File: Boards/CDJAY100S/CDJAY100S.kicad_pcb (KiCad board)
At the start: 2 copper layers, 150 x 185 mm, 54 parts, among them SW1 Rotary Encoder, U1 HT1632C-52LQFP

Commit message: Hide some details
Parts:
- moved C10 13.5 mm to (81.5, 32.1), turned to 90 degrees
- moved C9 11.0 mm to (86.0, 32.1), turned to 90 degrees
- moved R9 5.52 mm to (77.0, 32.0)
- moved R10 5.02 mm to (72.5, 32.0)
- moved R11 3.53 mm to (91.0, 32.0)
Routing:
- net Net-(rPi1-GPIO5): track 84.2 -> 96.7 mm
- net /GNDD: track 459.6 -> 447.1 mm
- net Net-(R11-Pad1): track 8.59 -> 12.5 mm
- net Net-(rPi1-GPIO4): track 87.6 -> 83.9 mm
- net Net-(rPi1-GPIO6): track 75.8 -> 72.3 mm
- net Net-(R9-Pad2): track 8.62 -> 7.10 mm
- net Net-(ControlJack1-Pin_2): track 77.8 -> 78.9 mm
- net Net-(ControlJack1-Pin_1): track 86.0 -> 87.0 mm

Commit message: Revision 1.1 of the PCB and Schematics.
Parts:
- removed C10, C9: 100 u, Capacitor_SMD:C_1206_3216Metric_Pad1.33x1.80mm_HandSolder
- removed C18: 47 u, Capacitor_SMD:C_1206_3216Metric_Pad1.33x1.80mm_HandSolder
- removed CR1: MBR120VLSFT1G, footprints:SDO_SOD-123FL_ONS
- removed Control: , Connector_Hirose:Hirose_DF13-02P-1.25DSA_1x02_P1.25mm_Vertical
- removed DSPB_Conn1: Conn_02x18_Odd_Even, 52045-3645:ConnectorFPC&FFC_MOL52045-3645-36P
- removed SW1: Rotary Encoder, Connector_PinHeader_2.54mm:PinHeader_1x05_P2.54mm_Vertical
- removed TB1: Conn_01x14, Connector_PinHeader_2.00mm:PinHeader_1x14_P2.00mm_Vertical
- added C22: 100 n, Capacitor_SMD:C_1206_3216Metric_Pad1.33x1.80mm_HandSolder, F.Cu at (161.5, 133.5)
- added C23: 100 n, Capacitor_SMD:C_1206_3216Metric_Pad1.33x1.80mm_HandSolder, F.Cu at (161.5, 129.5)
- added C24: 100 n, Capacitor_SMD:C_1206_3216Metric_Pad1.33x1.80mm_HandSolder, F.Cu at (168.5, 137.5)
- added C5: 100 u, Capacitor_SMD:C_1206_3216Metric_Pad1.33x1.80mm_HandSolder, F.Cu at (188.0, 82.4)
- added C6: 100 u, Capacitor_SMD:C_1206_3216Metric_Pad1.33x1.80mm_HandSolder, F.Cu at (188.0, 89.5)
- added CN701: 52492-3620, 52045-3645:ConnectorFPC&FFC_MOL52045-3645-36P_1, F.Cu at (193.5, 124.6)
- added CN705: 52151-1410, Connector_PinHeader_2.00mm:PinHeader_1x14_P2.00mm_Vertical, F.Cu at (194.0, 90.0)
- added D13: 1SS355VM, Diode_SMD:Nexperia_CFP3_SOD-123W, F.Cu at (169.5, 80.1)
- added D14: 1SS355VM, Diode_SMD:Nexperia_CFP3_SOD-123W, F.Cu at (164.5, 84.0)
- added D15: 1SS355VM, Diode_SMD:Nexperia_CFP3_SOD-123W, F.Cu at (169.5, 84.0)
- added D16: 1SS355VM, Diode_SMD:Nexperia_CFP3_SOD-123W, F.Cu at (164.5, 80.0)
- added J1: Rotary Encoder, Connector_PinHeader_2.54mm:PinHeader_1x05_P2.54mm_Vertical, F.Cu at (76.0, 25.0)
- added R21: 10k, Resistor_SMD:R_1206_3216Metric_Pad1.30x1.75mm_HandSolder, F.Cu at (140.5, 119.2)
- added R22: 10k, Resistor_SMD:R_1206_3216Metric_Pad1.30x1.75mm_HandSolder, F.Cu at (140.6, 122.5)
- added R23: 22k, Resistor_SMD:R_1206_3216Metric_Pad1.30x1.75mm_HandSolder, F.Cu at (182.5, 39.0)
- added R32: 10k, Resistor_SMD:R_1206_3216Metric_Pad1.30x1.75mm_HandSolder, F.Cu at (181.5, 71.5)
- added R33: 10k, Resistor_SMD:R_1206_3216Metric_Pad1.30x1.75mm_HandSolder, F.Cu at (185.0, 71.5)
- added R34: 10k, Resistor_SMD:R_1206_3216Metric_Pad1.30x1.75mm_HandSolder, F.Cu at (158.9, 85.5)
- added R7: 10k, Resistor_SMD:R_1206_3216Metric_Pad1.30x1.75mm_HandSolder, F.Cu at (140.5, 112.0)
- added R8: 10k, Resistor_SMD:R_1206_3216Metric_Pad1.30x1.75mm_HandSolder, F.Cu at (140.5, 115.5)
- C14, C15: value 1 u -> 2.2 u
- CR2: footprint footprints:SDO_SOD-123FL_ONS -> Diode_SMD:Nexperia_CFP3_SOD-123W
- D10, D11, D12, D8, D9: footprint Diode_SMD:D_SOD-323F -> Diode_SMD:Nexperia_CFP3_SOD-123W
- MH1, MH2, MH3, MH4: footprint MountingHole:MountingHole_2.2mm_M2 -> MountingHole:MountingHole_4.5mm
- R10, R11, R9: value 1 k -> 10 k
- R12: value 100 k -> 2k
- R13: value 10 k -> 2k
- R14: value 10 k -> 10k
- R15: value 100 -> 10k
- U1: value HT1632C-52LQFP -> PT6324Q; footprint Package_QFP:LQFP-52_14x14mm_P1mm -> Package_QFP:QFP-52_14x14mm_P1mm_1
- moved R14 68.5 mm to (159.0, 88.0)
- moved C16 56.4 mm to (196.5, 37.0)
- moved R13 55.1 mm to (158.5, 77.5), turned to -90 degrees
- moved R12 44.7 mm to (155.5, 77.5)
- moved CR2 44.7 mm to (183.4, 32.0), turned to 0 degrees
- moved R15 41.1 mm to (140.5, 126.0)
- moved C17 33.6 mm to (147.2, 90.5)
- moved R16 28.0 mm to (148.5, 104.5), turned to 90 degrees
- moved C12 25.3 mm to (147.2, 85.1), turned to -90 degrees
- moved R20 18.1 mm to (153.5, 159.1), turned to 90 degrees
- moved C14 17.7 mm to (189.5, 37.0), turned to 90 degrees
- moved C19 14.1 mm to (150.0, 111.0)
- moved C21 12.5 mm to (161.4, 137.5)
- moved R10 11.0 mm to (83.5, 32.0)
- moved R11 10.5 mm to (80.5, 32.0), turned to 90 degrees
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- renumbered SPi_Level1 to U2
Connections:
- net /GR12 renamed Net-(D12-A)
- net /GR13 renamed Net-(D11-A)
- net /GR14 renamed Net-(D10-A)
- net /GR15 renamed Net-(D8-A)
- net Net-(SPi_Level1-A4) renamed /SPI0 CS
- net Net-(SPi_Level1-A5) renamed /SPI0 SCK
- net Net-(SPi_Level1-A6) renamed /SPI0 RX
- net Net-(SPi_Level1-A7) renamed /SPI0 TX
- net Net-(rPi1-GPIO26_ADC0) renamed /ADIN
- C11 pad 1: Net-(SPi_Level1-A8) -> +3V3
- C12 pad 1: Net-(SPi_Level1-A8) -> +3V3
- C12 pad 2: /GNDD -> GND
- C13 pad 1: Net-(SPi_Level1-A8) -> +3V3
- C15 pad 2: GND -> GNDA
- C17 pad 1: Net-(DSPB_Conn1-Pin_36) -> +5V
- C17 pad 2: /GNDD -> GND
- C19 pad 2: /GNDD -> GND
- C20 pad 2: /GNDD -> GND
- C21 pad 1: /VDD -> +5V
- C21 pad 2: /GNDD -> GND
- CR2 pad 2: Net-(DSPB_Conn1-Pin_36) -> +5V
- R1 pad 1: Net-(DSPB_Conn1-Pin_34) -> Net-(R1-Pad1)
- R1 pad 2: Net-(R1-Pad2) -> Net-(CN701-ADIN)
- R10 pad 1: Net-(rPi1-GPIO5) -> +3V3
- R10 pad 2: Net-(R10-Pad2) -> Net-(J1-DT)
- R11 pad 1: Net-(R11-Pad1) -> +3V3
- R12 pad 1: Net-(rPi1-3V3_EN) -> Net-(rPi1-GPIO15)
- R12 pad 2: Net-(rPi1-VSYS) -> Net-(CN705-CONT1)
- R13 pad 1: Net-(rPi1-GPIO18) -> Net-(rPi1-GPIO22)
- R13 pad 2: /GNDD -> Net-(CN705-CONT2)
- R14 pad 1: Net-(rPi1-VBUS) -> Net-(CN705-CONT1)
- R14 pad 2: Net-(rPi1-GPIO18) -> +5V
- R15 pad 1: Net-(SPi_Level1-OE) -> Net-(D10-K)
- R15 pad 2: /GNDD -> GND
- R17 pad 2: /DOUT -> Net-(U1-DOUT)
- R18 pad 1: /GNDD -> GND
- R19 pad 1: /VDD -> /DOUT
- R19 pad 2: /DOUT -> +5V
- R2 pad 1: Net-(R1-Pad2) -> Net-(R1-Pad1)
- R20 pad 1: /GNDD -> GND
- R3 pad 1: Net-(R1-Pad2) -> Net-(R1-Pad1)
- R5 pad 1: Net-(DSPB_Conn1-Pin_35) -> Net-(R4-Pad1)
- R5 pad 2: Net-(R4-Pad1) -> Net-(CN701-CT)
- R9 pad 1: Net-(rPi1-GPIO4) -> Net-(J1-CLK)
- R9 pad 2: Net-(R9-Pad2) -> +3V3
- U1 pad 10: /SG1 -> Net-(CN701-S1)
- U1 pad 11: /SG2 -> Net-(CN701-S2)
- U1 pad 12: /SG3 -> Net-(CN701-S3)
- U1 pad 13: /SG4 -> Net-(CN701-S4)
- U1 pad 14: /SG5 -> Net-(CN701-S5)
- U1 pad 15: /SG6 -> Net-(CN701-S6)
- U1 pad 17: /SG8 -> Net-(CN701-S8)
- U1 pad 18: /SG9 -> Net-(CN701-S9)
- U1 pad 19: /SG10 -> Net-(CN701-S10)
- U1 pad 20: /SG11 -> Net-(CN701-S11)
- U1 pad 21: /SG12 -> Net-(CN701-S12)
- U1 pad 34: /GR1 -> Net-(CN701-G1)
- U1 pad 35: /GR2 -> Net-(CN701-G2)
- U1 pad 36: /GR3 -> Net-(CN701-G3)
- U1 pad 37: /GR4 -> Net-(CN701-G4)
- U1 pad 38: /GR5 -> Net-(CN701-G5)
- U1 pad 39: /GR6 -> Net-(CN701-G6)
- U1 pad 4: /DOUT -> Net-(U1-DOUT)
- U1 pad 40: /GR7 -> Net-(CN701-G7)
- U1 pad 41: /GR8 -> Net-(CN701-G8)
- U1 pad 42: /GR9 -> Net-(CN701-G9)
- U1 pad 43: /GR10 -> Net-(CN701-G10)
- U1 pad 44: /GR11 -> Net-(CN701-G11)
- U1 pad 50: Net-(TB1-Pin_12) -> Vload
- U1 pad 51: /VDD -> +5V
- U1 pad 52: /GNDD -> GND
- U1 pad 8: /GNDD -> GND
- U1 pad 9: /VDD -> +5V
- U2 pad 10: Net-(SPi_Level1-OE) -> +3V3
- U2 pad 11: /GNDD -> GND
- U2 pad 12: /VDD -> unconnected-(U2-B8-Pad12)
- U2 pad 19: Net-(DSPB_Conn1-Pin_36) -> +5V
- U2 pad 2: Net-(SPi_Level1-A8) -> +3V3
- U2 pad 9: Net-(SPi_Level1-A8) -> unconnected-(U2-A8-Pad9)
- i2S_Audio1 pad 11: GND -> +3V3
- i2S_Audio1 pad 9: GND -> GNDA
- rPi1 pad 13: /GNDD -> GND
- rPi1 pad 18: /GNDD -> GND
- rPi1 pad 20: Net-(ControlJack1-Pin_1) -> Net-(rPi1-GPIO15)
- rPi1 pad 23: /GNDD -> GND
- rPi1 pad 24: Net-(rPi1-GPIO18) -> unconnected-(rPi1-GPIO18-Pad24)
- rPi1 pad 25: Net-(i2S_Audio1-LRCK) -> Net-(i2S_Audio1-BCK)
- rPi1 pad 26: Net-(i2S_Audio1-DIN) -> Net-(i2S_Audio1-LRCK)
- rPi1 pad 27: Net-(i2S_Audio1-BCK) -> Net-(i2S_Audio1-DIN)
- rPi1 pad 28: /GNDD -> GND
- rPi1 pad 29: Net-(ControlJack1-Pin_2) -> Net-(rPi1-GPIO22)
- rPi1 pad 3: /GNDD -> GND
- rPi1 pad 36: Net-(SPi_Level1-A8) -> +3V3
- rPi1 pad 37: Net-(rPi1-3V3_EN) -> unconnected-(rPi1-3V3_EN-Pad37)
- rPi1 pad 38: /GNDD -> GND
- rPi1 pad 40: Net-(rPi1-VBUS) -> unconnected-(rPi1-VBUS-Pad40)
- rPi1 pad 6: Net-(rPi1-GPIO4) -> Net-(J1-DT)
- rPi1 pad 7: Net-(rPi1-GPIO5) -> Net-(J1-CLK)
- rPi1 pad 8: /GNDD -> GND
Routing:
- net /GNDD: track 447.1 -> 0.00 mm, vias 4 -> 0
- net GND: track 188.3 -> 571.4 mm, vias 1 -> 12
- net +5V: track 0.00 -> 280.4 mm, vias 0 -> 5
- net +3V3: track 0.00 -> 225.2 mm, vias 0 -> 5
- net Net-(DSPB_Conn1-Pin_36): track 220.1 -> 0.00 mm, vias 3 -> 0
- net /VDD: track 134.5 -> 0.00 mm, vias 3 -> 0
- net Net-(SPi_Level1-A8): track 117.8 -> 0.00 mm, vias 1 -> 0
- net Net-(rPi1-GPIO5): track 96.7 -> 0.00 mm, vias 1 -> 0
- net Net-(TB1-Pin_12): track 94.6 -> 0.00 mm, vias 1 -> 0
- net Net-(ControlJack1-Pin_1): track 87.0 -> 0.00 mm
- net Vload: track 0.00 -> 85.0 mm, vias 0 -> 1
- net Net-(rPi1-GPIO18): track 84.3 -> 0.00 mm, vias 1 -> 0
- net Net-(J1-DT): track 0.00 -> 84.0 mm
- net Net-(rPi1-GPIO4): track 83.9 -> 0.00 mm, vias 1 -> 0
- net Net-(J1-CLK): track 0.00 -> 79.0 mm
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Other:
- outline, holes or cut-outs redrawn
- board text added: "CDJay 100 USB Mainboard V1.1 applab.fh-aachen.de Write it, load it, run it, save it Check it, change it, quick - reuse it"
- board text removed: "CDJay 100 USB Mainboard V1.0 applab.fh-aachen.de Write it, cut it, paste it, save it Load it, check it, quick - rewrite it"

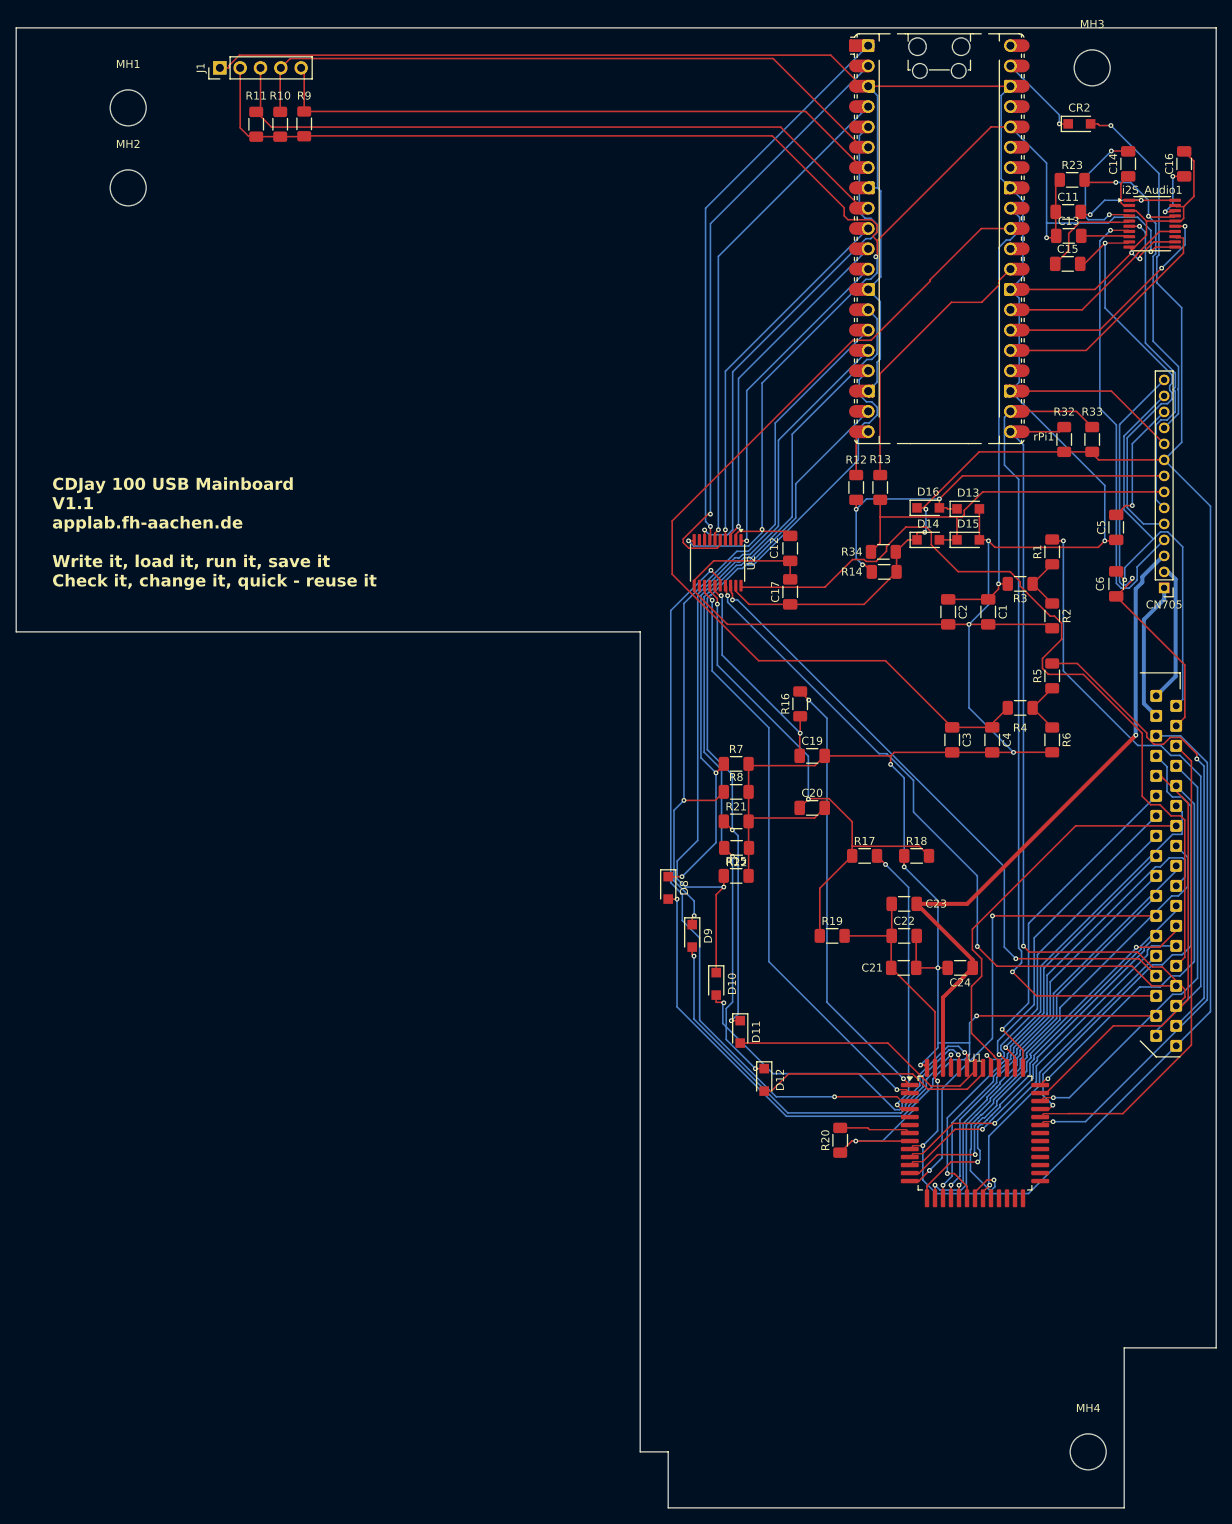
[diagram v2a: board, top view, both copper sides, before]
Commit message: Include USB-Hub
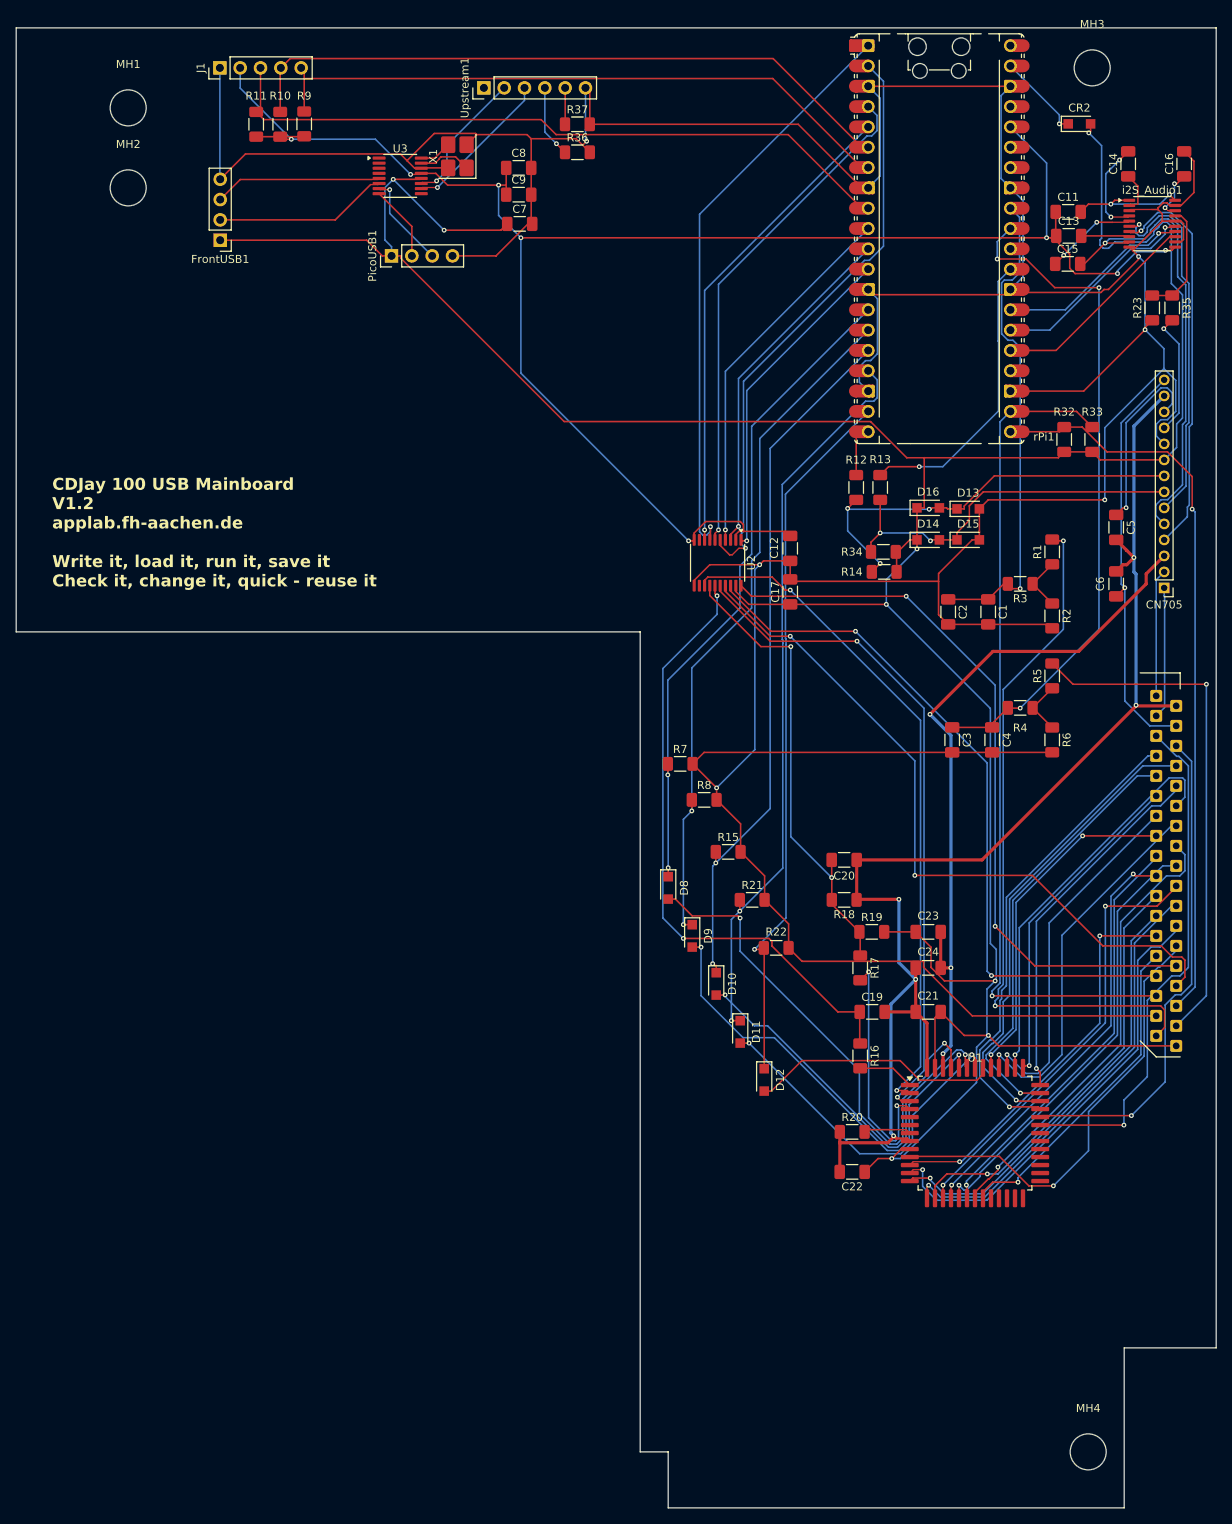
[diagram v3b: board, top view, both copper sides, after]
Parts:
- added C7: 10u, Capacitor_SMD:C_1206_3216Metric_Pad1.33x1.80mm_HandSolder, F.Cu at (113.4, 44.5)
- added C8: 10u, Capacitor_SMD:C_1206_3216Metric_Pad1.33x1.80mm_HandSolder, F.Cu at (113.3, 37.5)
- added C9: 1uf, Capacitor_SMD:C_1206_3216Metric_Pad1.33x1.80mm_HandSolder, F.Cu at (113.3, 40.9)
- added FrontUSB1: Conn_01x04_Pin, Connector_PinHeader_2.54mm:PinHeader_1x04_P2.54mm_Vertical, F.Cu at (76.0, 46.5)
- added PicoUSB1: Conn_01x04_Pin, Connector_PinHeader_2.54mm:PinHeader_1x04_P2.54mm_Vertical, F.Cu at (97.4, 48.5)
- added R35: 10k, Resistor_SMD:R_1206_3216Metric_Pad1.30x1.75mm_HandSolder, F.Cu at (195.0, 55.0)
- added R36: 5.1 k, Resistor_SMD:R_1206_3216Metric_Pad1.30x1.75mm_HandSolder, F.Cu at (120.7, 35.5)
- added R37: 5 k, Resistor_SMD:R_1206_3216Metric_Pad1.30x1.75mm_HandSolder, F.Cu at (120.7, 32.0)
- added U3: CH334R, Package_SO:QSOP-16_3.9x4.9mm_P0.635mm, F.Cu at (98.5, 38.5)
- added Upstream1: Conn_01x06_Pin, Connector_PinHeader_2.54mm:PinHeader_1x06_P2.54mm_Vertical, F.Cu at (109.0, 27.5)
- added X1: 12MHz, Crystal:Crystal_SMD_3225-4Pin_3.2x2.5mm_HandSoldering, F.Cu at (105.7, 36.0)
- R23: value 22k -> 20k
- R3, R4: value 5 k -> 5.1 k
- moved R16 44.6 mm to (156.0, 148.5), turned to -90 degrees
- moved C19 32.9 mm to (157.5, 143.0)
- moved C22 30.2 mm to (155.0, 163.0), turned to 180 degrees
- moved R23 18.9 mm to (192.5, 55.0), turned to 90 degrees
- moved R17 14.0 mm to (156.0, 137.5), turned to -90 degrees
- moved R22 13.4 mm to (145.5, 135.0)
- moved R18 10.6 mm to (154.0, 129.0), turned to 180 degrees
- moved R21 10.0 mm to (142.5, 129.0)
- moved C20 7.63 mm to (154.0, 124.0)
- moved R7 7.00 mm to (133.5, 112.0)
- moved C21 6.30 mm to (164.5, 143.0), turned to 180 degrees
- moved R19 4.98 mm to (157.4, 133.0)
- moved C23 4.61 mm to (164.5, 133.0)
- moved R8 4.12 mm to (136.5, 116.5)
- moved C24 4.00 mm to (164.5, 137.5)
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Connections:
- net AC1 renamed Net-(CN701-AC1)
- net AC2 renamed Net-(CN701-AC2)
- C19 pad 2: GND -> GNDS
- C20 pad 2: GND -> GNDS
- C21 pad 2: GND -> GNDS
- C22 pad 2: GND -> GNDS
- C24 pad 2: GND -> GNDS
- C5 pad 1: GND -> V+BV
- C5 pad 2: V+BV -> GNDS
- R18 pad 1: GND -> GNDS
- R20 pad 1: GND -> GNDS
- R23 pad 1: +3V3 -> GND
- R23 pad 2: Net-(CN705-/RST) -> Net-(i2S_Audio1-XSMT)
- U1 pad 52: GND -> GNDS
- U1 pad 8: GND -> GNDS
- i2S_Audio1 pad 17: Net-(CN705-/RST) -> Net-(i2S_Audio1-XSMT)
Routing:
- net +5V: track 280.4 -> 410.0 mm, vias 5 -> 8
- net GNDS: track 54.6 -> 168.1 mm, vias 1 -> 5
- net /CLK: track 27.9 -> 78.2 mm
- net Net-(U1-CLK): track 54.9 -> 7.07 mm, vias 2 -> 0
- net /ADIN: track 116.2 -> 85.9 mm, vias 0 -> 3
- net Net-(CN705-/RST): track 43.5 -> 15.4 mm, vias 2 -> 1
- net Net-(FrontUSB1-D+): track 0.00 -> 21.7 mm
- net Net-(FrontUSB1-D-): track 0.00 -> 21.0 mm
- net GND: track 571.4 -> 592.1 mm, vias 12 -> 6
- net Net-(U3-DMU-): track 0.00 -> 19.0 mm, vias 0 -> 1
- net Net-(U3-DPU+): track 0.00 -> 17.2 mm, vias 0 -> 1
- net Net-(i2S_Audio1-XSMT): track 0.00 -> 14.2 mm
- net /KD0: track 105.6 -> 91.7 mm, vias 0 -> 2
- net Net-(CN701-ADIN): track 75.1 -> 88.2 mm, vias 1 -> 2
- net Net-(PicoUSB1-D-): track 0.00 -> 11.9 mm, vias 0 -> 1
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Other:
- board text added: "CDJay 100 USB Mainboard V1.2 applab.fh-aachen.de Write it, load it, run it, save it Check it, change it, quick - reuse it"
- board text removed: "CDJay 100 USB Mainboard V1.1 applab.fh-aachen.de Write it, load it, run it, save it Check it, change it, quick - reuse it"

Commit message: Board Revision 1.4
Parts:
- removed C20: 100 p, Capacitor_SMD:C_1206_3216Metric_Pad1.33x1.80mm_HandSolder
- removed R17: 470, Resistor_SMD:R_1206_3216Metric_Pad1.30x1.75mm_HandSolder
- removed R18: 10 k, Resistor_SMD:R_1206_3216Metric_Pad1.30x1.75mm_HandSolder
- removed R19: 1 k, Resistor_SMD:R_1206_3216Metric_Pad1.30x1.75mm_HandSolder
- R37: value 5 k -> 5.1 k
- moved U1 31.3 mm to (171.5, 126.8), turned to 90 degrees
- moved C22 28.9 mm to (175.5, 142.6), turned to -90 degrees
- moved R20 22.2 mm to (171.0, 142.6), turned to 90 degrees
- moved D11 18.6 mm to (141.0, 126.9)
- moved D12 18.6 mm to (144.0, 132.9)
- moved D10 18.5 mm to (138.0, 121.0)
- moved D8 18.5 mm to (132.0, 109.0)
- moved D9 18.5 mm to (135.0, 115.0)
- moved R22 14.5 mm to (145.5, 120.5)
- moved C24 14.3 mm to (153.0, 129.0), turned to -90 degrees
- moved R21 13.0 mm to (142.5, 116.0)
- moved R15 12.0 mm to (139.5, 111.0)
- moved C21 11.6 mm to (156.5, 134.6), turned to -90 degrees
- moved R16 11.3 mm to (163.5, 140.0), turned to 0 degrees
- moved R7 10.5 mm to (133.5, 101.5)
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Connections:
- U1 pad 4: Net-(U1-DOUT) -> unconnected-(U1-DOUT-Pad4)
- U1 pad 45: Net-(D12-A) -> Net-(D8-A)
- U1 pad 46: Net-(D11-A) -> Net-(D9-A)
- U1 pad 48: Net-(D9-A) -> Net-(D11-A)
- U1 pad 49: Net-(D8-A) -> Net-(D12-A)
- U2 pad 14: /DOUT -> unconnected-(U2-B6-Pad14)
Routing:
- net +5V: track 410.0 -> 350.9 mm, vias 8 -> 6
- net /DOUT: track 58.4 -> 0.00 mm, vias 2 -> 0
- net Net-(CN701-S5): track 56.0 -> 17.1 mm, vias 1 -> 0
- net Net-(CN701-S11): track 56.4 -> 17.9 mm, vias 1 -> 0
- net Net-(CN701-S6): track 53.0 -> 14.7 mm, vias 1 -> 0
- net Net-(CN701-S8): track 52.9 -> 14.9 mm, vias 2 -> 0
- net Net-(CN701-G1): track 64.9 -> 27.2 mm, vias 1 -> 0
- net Net-(CN701-S9): track 55.2 -> 17.5 mm, vias 1 -> 0
- net Net-(CN701-S7): track 54.9 -> 17.3 mm, vias 2 -> 0
- net Net-(CN701-S10): track 52.7 -> 15.3 mm, vias 1 -> 0
- net Net-(CN701-S4): track 54.0 -> 17.2 mm, vias 1 -> 0
- net Net-(CN701-S3): track 57.4 -> 21.8 mm, vias 1 -> 0
- net Net-(CN701-S1): track 56.0 -> 24.2 mm, vias 1 -> 0
- net Net-(U1-DOUT): track 30.7 -> 0.00 mm, vias 2 -> 0
- net Net-(CN701-G3): track 59.2 -> 29.2 mm
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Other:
- board text added: "CDJay 100 USB Mainboard V1.4 applab.fh-aachen.de Write it, load it, run it, save it Check it, change it, quick - reuse it"
- board text removed: "CDJay 100 USB Mainboard V1.2 applab.fh-aachen.de Write it, load it, run it, save it Check it, change it, quick - reuse it"

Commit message: Board Revision 1.5
Only cosmetic changes
- Fixed the footprint of the 36p connector to remove the bottom screen covering the copper
- Added a solder jumper to connect the /rst pin to the pico if needed
- moved MH3 down 0.5mm
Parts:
- added JP1: , Jumper:SolderJumper-2_P1.3mm_Open_Pad1.0x1.5mm, B.Cu at (178.8, 31.9)
- moved CR2 1.25 mm to (183.5, 33.2)
- moved MH3 1.00 mm to (185.0, 26.0)
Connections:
- rPi1 pad 37: unconnected-(rPi1-3V3_EN-Pad37) -> Net-(JP1-A)
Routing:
- net Net-(JP1-B): track 14.0 -> 41.4 mm
- net Net-(JP1-A): track 0.00 -> 5.18 mm, vias 0 -> 1
- net GND: track 585.9 -> 588.8 mm
- net +3V3: track 222.9 -> 220.6 mm
- net +5V: track 350.9 -> 352.6 mm, vias 6 -> 5
- net Net-(D8-K): track 65.0 -> 63.6 mm
- net Net-(rPi1-VSYS): track 10.7 -> 12.0 mm
- net unconnected-(rPi1-3V3_EN-Pad37): track 0.80 -> 0.00 mm
- net V+BV: track 20.0 -> 20.6 mm
- net Net-(PicoUSB1-D+): track 9.47 -> 9.98 mm
- net Net-(PicoUSB1-D-): vias 1 -> 0
- net Net-(Upstream1-CC1): vias 1 -> 0
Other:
- board text added: "CDJay 100 USB Mainboard V1.5 applab.fh-aachen.de Write it, load it, run it, save it Check it, change it, quick - reuse it"
- board text removed: "CDJay 100 USB Mainboard V1.4 applab.fh-aachen.de Write it, load it, run it, save it Check it, change it, quick - reuse it"
